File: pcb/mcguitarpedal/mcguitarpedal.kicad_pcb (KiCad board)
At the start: 2 copper layers, 129.5 x 123 mm, 73 parts, among them J1 IN, J10 ENCODER2, J11 ENCODER3, J2 PREAMP_HEADERS, J3 BTN_MTX, J4 OUT, J5 EXP, J6 ILI9488 Module, J7 PWR_IN, J8 POT_HP_VOLUME_10k, J9 ENCODER1, SW1 SW_BYPASS, SW3 SW_PRESET, SW4 LINE_LEVEL, SW5 SW_TUNER, SW6 SW_PRESET, U2 Teensy4.1, U3 LM4562, U4 74HC148, U5 74HC4094, U6 STPDWN-3P-5V, U7 STDN-3A24-ADJ

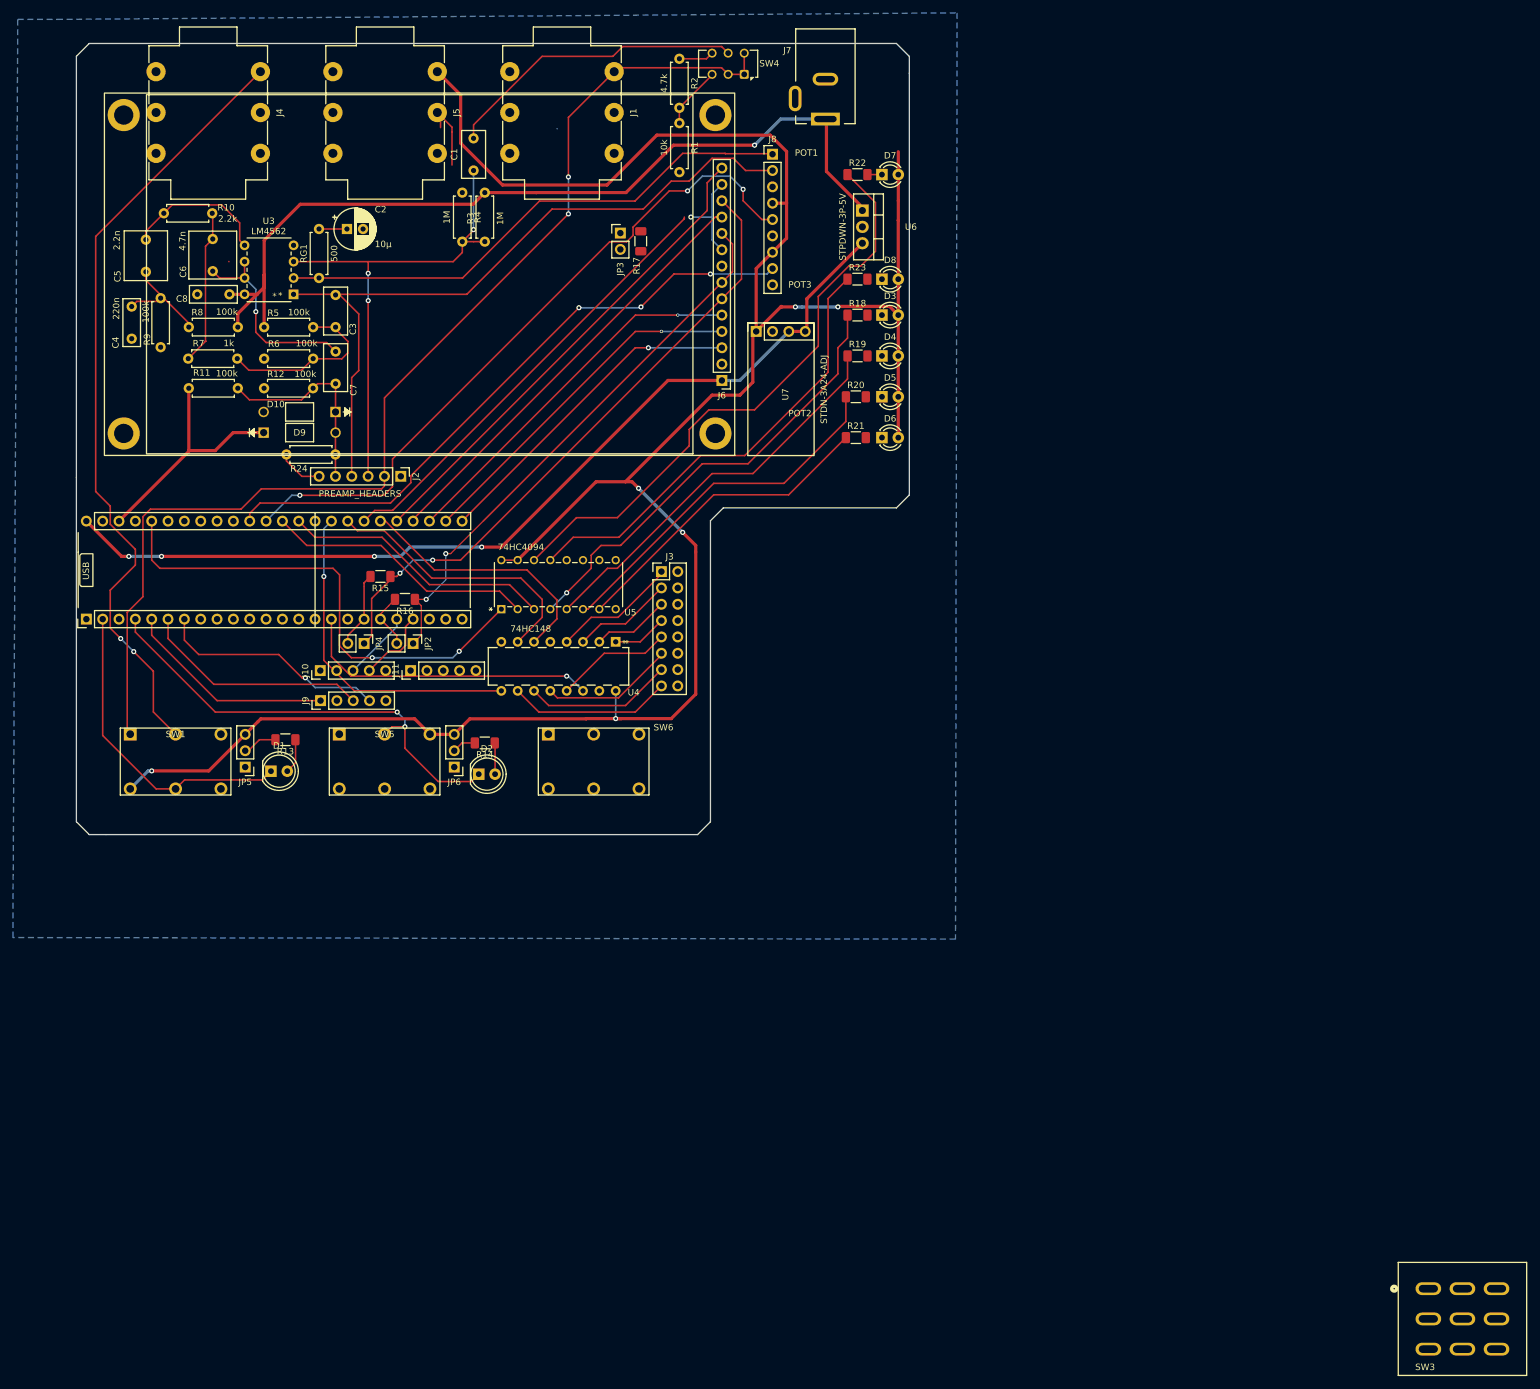
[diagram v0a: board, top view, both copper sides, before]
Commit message: HCT595, audio shield sockets
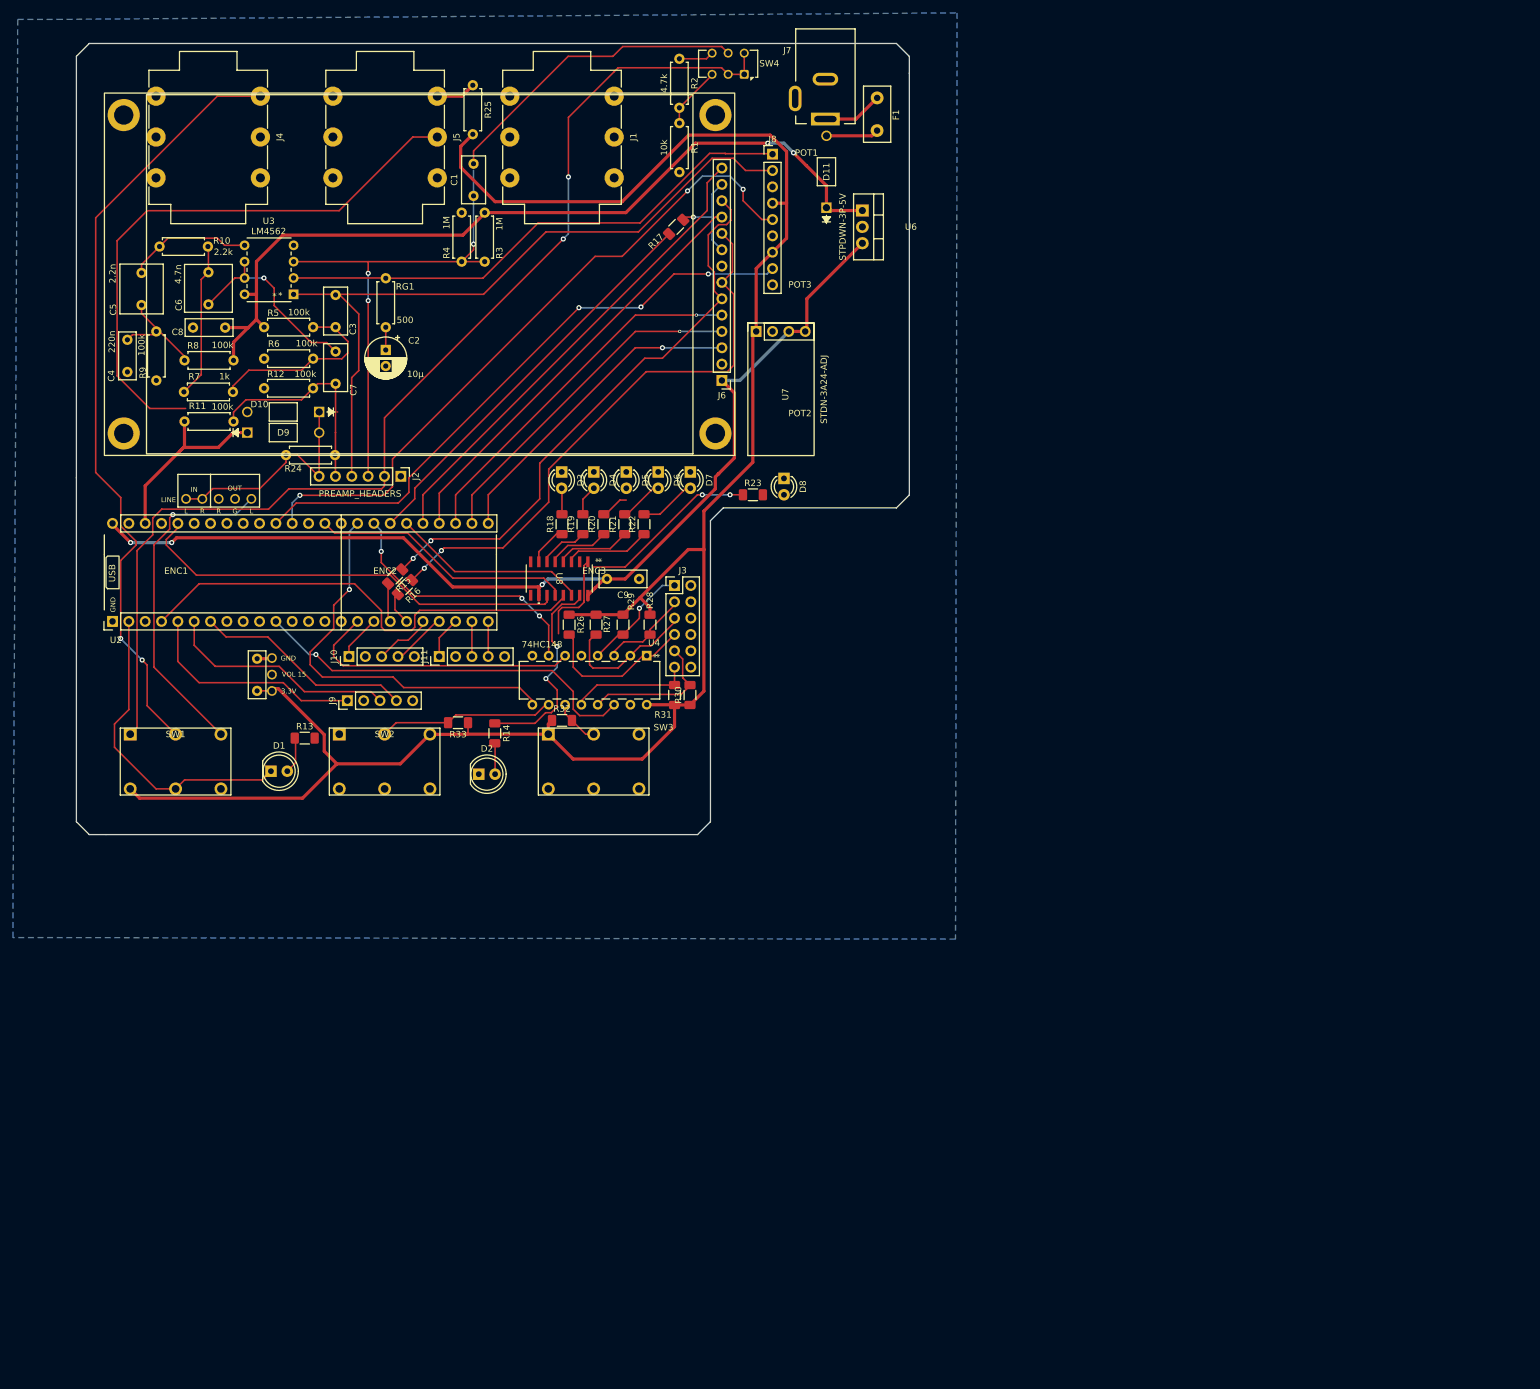
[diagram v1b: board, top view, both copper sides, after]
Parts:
- removed JP2: JP_SCLK, Connector_PinHeader_2.54mm:PinHeader_1x02_P2.54mm_Vertical
- removed JP3: JP_MISO, Connector_PinHeader_2.54mm:PinHeader_1x02_P2.54mm_Vertical
- removed JP4: JP_MOSI, Connector_PinHeader_2.54mm:PinHeader_1x02_P2.54mm_Vertical
- removed JP5, JP6: JP_SW1_LED, Connector_PinHeader_2.54mm:PinHeader_1x03_P2.54mm_Vertical
- removed the R21 at (170.7, 81.3)
- removed the SW3 at (259.7, 213.6)
- removed U5: 74HC4094, TI_FOOTPRINTS:N16
- added C10: 100nf, Capacitor_THT:C_Rect_L7.2mm_W2.5mm_P5.00mm_FKS2_FKP2_MKS2_MKP2, F.Cu at (77.6, 120.7)
- added C9: 100nf, Capacitor_THT:C_Rect_L7.2mm_W2.5mm_P5.00mm_FKS2_FKP2_MKS2_MKP2, F.Cu at (137.0, 103.3)
- added D11: D_Schottky, TI_FOOTPRINTS:DO-41_DIO, F.Cu at (166.1, 45.5)
- added ENC1: Logo_Open_Hardware_Small, mcguitarpedal:Floating Encoder, F.Cu at (65.0, 102.5)
- added ENC2: Logo_Open_Hardware_Small, mcguitarpedal:Floating Encoder, F.Cu at (97.5, 102.5)
- added ENC3: Logo_Open_Hardware_Small, mcguitarpedal:Floating Encoder, F.Cu at (130.0, 102.5)
- added F1: Fuse 1A, Fuse:Fuse_Littelfuse_395Series, F.Cu at (174.0, 28.5)
- added R18: 330, Resistor_SMD:R_1206_3216Metric_Pad1.30x1.75mm_HandSolder, F.Cu at (125.0, 94.7)
- added R25: 1k, Resistor_THT:R_Axial_DIN0207_L6.3mm_D2.5mm_P7.62mm_Horizontal, F.Cu at (111.1, 26.5)
- added R26: 10k, Resistor_SMD:R_1206_3216Metric_Pad1.30x1.75mm_HandSolder, F.Cu at (126.1, 110.4)
- added R27: 10k, Resistor_SMD:R_1206_3216Metric_Pad1.30x1.75mm_HandSolder, F.Cu at (130.3, 110.4)
- added R28: 10k, Resistor_SMD:R_1206_3216Metric_Pad1.30x1.75mm_HandSolder, F.Cu at (138.7, 110.4)
- added R29: 10k, Resistor_SMD:R_1206_3216Metric_Pad1.30x1.75mm_HandSolder, F.Cu at (134.5, 110.4)
- added R30: 10k, Resistor_SMD:R_1206_3216Metric_Pad1.30x1.75mm_HandSolder, F.Cu at (144.9, 121.3)
- added R31: 10k, Resistor_SMD:R_1206_3216Metric_Pad1.30x1.75mm_HandSolder, F.Cu at (142.5, 121.3)
- added R32: 10k, Resistor_SMD:R_1206_3216Metric_Pad1.30x1.75mm_HandSolder, F.Cu at (125.0, 125.2)
- added R33: 10k, Resistor_SMD:R_1206_3216Metric_Pad1.30x1.75mm_HandSolder, F.Cu at (108.8, 125.6)
- added U2: Teensy Audio Board, mcguitarpedal:4.0audioshield, F.Cu at (55.1, 109.9)
- added U8: 74HCT595D, TI_FOOTPRINTS:SOT109-1_NEX, F.Cu at (124.6, 103.2)
- D3, D6, D7, D8: footprint LED_THT:LED_D3.0mm -> mcguitarpedal:LED_D3.0mm
- D4: renamed from D5; footprint LED_THT:LED_D3.0mm -> mcguitarpedal:LED_D3.0mm
- D5: renamed from D4; footprint LED_THT:LED_D3.0mm -> mcguitarpedal:LED_D3.0mm
- J3: footprint Connector_PinHeader_2.54mm:PinHeader_2x08_P2.54mm_Vertical -> Connector_PinHeader_2.54mm:PinHeader_2x06_P2.54mm_Vertical
- J6: footprint ILI9488:ILI9488 -> mcguitarpedal:ILI9488
- R13, R14, R22, R23: value 150 -> 330
- R19: renamed from R20; value 150 -> 330
- R20: renamed from R19; value 150 -> 330
- R21: renamed from R18; value 150 -> 330
- moved R22 63.7 mm to (137.8, 94.7), turned to 90 degrees
- moved D3 55.4 mm to (125.0, 86.6), turned to -90 degrees
- moved D7 55.0 mm to (145.0, 86.6), turned to -90 degrees
- moved R21 48.7 mm to (134.8, 94.7), turned to 90 degrees
- moved R20 47.3 mm to (131.5, 94.7), turned to 90 degrees
- moved R19 46.8 mm to (128.2, 94.7), turned to 90 degrees
- moved D4 46.3 mm to (130.0, 86.6), turned to -90 degrees
- moved D5 43.6 mm to (135.0, 86.6), turned to -90 degrees
- moved R23 37.3 mm to (154.7, 90.2)
- moved D6 35.2 mm to (140.0, 86.6), turned to -90 degrees
- moved D8 34.5 mm to (159.5, 87.6), turned to -90 degrees
- moved C2 19.8 mm to (97.6, 67.7), turned to -90 degrees
- moved RG1 10.4 mm to (97.6, 56.5), turned to -90 degrees
- moved R17 5.94 mm to (142.7, 48.5), turned to -135 degrees
- moved U4 5.29 mm to (138.2, 115.2)
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- renumbered SW5 to SW2, SW6 to SW3, U2 to U1
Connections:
- net Net-(U2-40_A16) renamed /40_BTN_MTX_B
- net Net-(U2-41_A17) renamed /41_BTN_MTX_A
- D1 pad 1: /1_SW1 -> GND
- D10 pad 1: /preamp/PREAMP_OUT -> /LINE_IN
- D2 pad 1: /2_SW2 -> GND
- D3 pad 1: Net-(D3-K) -> GND
- D3 pad 2: 3.3V -> Net-(D3-A)
- D4 pad 1: Net-(D5-K) -> GND
- D4 pad 2: 3.3V -> Net-(D4-A)
- D5 pad 1: Net-(D4-K) -> GND
- D5 pad 2: 3.3V -> Net-(D5-A)
- D6 pad 1: Net-(D6-K) -> GND
- D6 pad 2: 3.3V -> Net-(D6-A)
- D7 pad 1: Net-(D7-K) -> GND
- D7 pad 2: 3.3V -> Net-(D7-A)
- D8 pad 1: Net-(D8-K) -> GND
- D8 pad 2: 3.3V -> Net-(D8-A)
- D9 pad 2: /preamp/PREAMP_OUT -> /LINE_IN
- J5 pad T: 3.3V -> Net-(J5-PadT)
- J7 pad 1: 9V -> Net-(F1-Pad1)
- J7 pad 3: (no net) -> unconnected-(J7-Pad3)
- R14 pad 1: Net-(D2-A) -> Net-(U8-Q0)
- R14 pad 2: Net-(JP6-C) -> Net-(D2-A)
- R19 pad 2: Net-(D5-K) -> Net-(D4-A)
- R20 pad 2: Net-(D4-K) -> Net-(D5-A)
- R21 pad 2: Net-(D3-K) -> Net-(D6-A)
- R22 pad 2: Net-(D7-K) -> Net-(D7-A)
- R23 pad 2: Net-(D8-K) -> Net-(D8-A)
- SW2 pad 2: /2_SW2 -> /SW2
- SW3 pad 1: unconnected-(SW6-A-Pad1) -> 3.3V
- SW3 pad 2: unconnected-(SW6-B-Pad2) -> /SW3
- SW3 pad 3: unconnected-(SW6-C-Pad3) -> GND
- U1 pad 10: Net-(U2-8_TX2_IN1) -> unconnected-(U1-8_TX2_IN1-Pad10)
- U1 pad 11: Net-(U2-9_OUT1C) -> /24_BTN_MTX_GS
- U1 pad 12: Net-(U2-10_CS_MQSR) -> unconnected-(U1-10_CS_MQSR-Pad12)
- U1 pad 13: Net-(U2-11_MOSI_CTX1) -> unconnected-(U1-11_MOSI_CTX1-Pad13)
- U1 pad 14: Net-(U2-12_MISO_MQSL) -> unconnected-(U1-12_MISO_MQSL-Pad14)
- U1 pad 16: /24_BTN_MTX_GS -> /24_BTN_MTX_C
- U1 pad 3: Net-(U2-1_TX1_CTX2_MISO1) -> unconnected-(U1-1_TX1_CTX2_MISO1-Pad3)
- U1 pad 30: Net-(U2-38_CS1_IN1) -> /38_LED_DATA
- U1 pad 36: /LED_DATA -> /14_BACKLIGHT_PWM
- U1 pad 4: /2_SW2 -> /2_LED_PWM
- U1 pad 8: Net-(U2-6_OUT1D) -> unconnected-(U1-6_OUT1D-Pad8)
- U1 pad 9: Net-(U2-7_RX2_OUT1A) -> unconnected-(U1-7_RX2_OUT1A-Pad9)
- U4 pad 10: Net-(J3-Pin_15) -> /SW2
- U4 pad 11: Net-(J3-Pin_13) -> /SW3
- U4 pad 15: GND -> unconnected-(U4-EO-Pad15)
- U4 pad 6: Net-(U2-38_CS1_IN1) -> /24_BTN_MTX_C
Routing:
- net Net-(U8-Q3): track 93.0 -> 13.4 mm
- net /A3_EXP: track 11.3 -> 90.2 mm
- net /2_LED_PWM: track 0.00 -> 73.0 mm
- net /2_SW2: track 71.7 -> 0.00 mm, vias 2 -> 0
- net Net-(U8-Q4): track 70.8 -> 11.7 mm, vias 1 -> 0
- net 3.3V: track 370.7 -> 312.7 mm, vias 6 -> 0
- net /LINE_OUT: track 0.00 -> 52.9 mm, vias 0 -> 1
- net Net-(U8-Q5): track 62.1 -> 9.68 mm
- net Net-(U5-QP3): track 49.4 -> 0.00 mm
- net Net-(U8-Q6): track 56.8 -> 8.39 mm
- net /24_BTN_MTX_C: track 0.00 -> 44.2 mm
- net Net-(U8-Q2): track 71.0 -> 28.0 mm, vias 0 -> 2
- net /LED_DATA: track 42.3 -> 0.00 mm
- net Net-(U2-38_CS1_IN1): track 40.5 -> 0.00 mm
- net Net-(U8-Q0): track 0.00 -> 32.8 mm, vias 0 -> 2
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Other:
- board text added: "TODO: Audio board sockets for line in/out and 3V3 PWR LEDs LED PWM Testpoints Mounting holes Footswitch pushbutton Move 5V regulator above U5 Change diode footprint Header silkscreen labels Move jacks down to reduce board size vertically Move Teensy right to reduce board size horizontally Use SMD HC148? Use HCT595 instead of 4094 Route SW2 to BTN_MTX Decoupling caps for U4-7"
- board text removed: "TODO: Audio board 3V3 PWR LEDs Testpoints Encoders Evenly distribute jacks Mounting holes Footswitch pushbutton Switch 470n to smaller footprint Move 5V regulator above U5"

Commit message: Miniaturization
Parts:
- added R34: 10k, Resistor_SMD:R_1206_3216Metric_Pad1.30x1.75mm_HandSolder, F.Cu at (70.8, 46.5)
- added R35: 10k, Resistor_SMD:R_1206_3216Metric_Pad1.30x1.75mm_HandSolder, F.Cu at (58.0, 49.0)
- added SW5: SW_PWR, Connector_PinHeader_2.54mm:PinHeader_1x02_P2.54mm_Vertical, F.Cu at (166.2, 25.2)
- R1: footprint Resistor_THT:R_Axial_DIN0207_L6.3mm_D2.5mm_P7.62mm_Horizontal -> Resistor_SMD:R_1206_3216Metric_Pad1.30x1.75mm_HandSolder
- R2: value 4.7k -> 10k; footprint Resistor_THT:R_Axial_DIN0207_L6.3mm_D2.5mm_P7.62mm_Horizontal -> Resistor_SMD:R_1206_3216Metric_Pad1.30x1.75mm_HandSolder
- SW4: footprint Button_Switch_THT:SW_CK_JS202011AQN_DPDT_Angled -> mcguitarpedal:DP3T slide switch
- U6: footprint Package_TO_SOT_THT:TO-220-3_Vertical -> Package_TO_SOT_THT:TO-220-3_Horizontal_TabDown
- moved SW4 95.5 mm to (61.2, 49.9), turned to 90 degrees
- moved R2 87.7 mm to (58.0, 43.0)
- moved R1 85.4 mm to (58.0, 37.5)
- moved R23 57.7 mm to (176.0, 36.5), turned to 90 degrees
- moved D8 57.6 mm to (173.5, 31.7), turned to 0 degrees
- moved R25 51.4 mm to (162.0, 34.2)
- moved C1 35.8 mm to (76.4, 52.0), turned to 180 degrees
- moved R3 23.3 mm to (90.0, 49.8)
- moved D9 20.4 mm to (57.2, 88.4)
- moved D10 20.4 mm to (68.4, 85.0)
- moved R4 13.0 mm to (96.9, 57.4)
- moved J4 12.1 mm to (90.2, 27.9)
- moved C4 12.0 mm to (66.2, 74.2), turned to 180 degrees
- moved J5 8.59 mm to (114.2, 28.2)
- moved R9 7.31 mm to (67.5, 69.5), turned to 180 degrees
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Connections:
- C1 pad 2: Net-(C1-Pad2) -> Net-(SW4-D)
- F1 pad 1: Net-(F1-Pad1) -> Net-(SW5-B)
- J7 pad 1: Net-(F1-Pad1) -> Net-(SW5-A)
- R1 pad 1: Net-(R1-Pad1) -> GND
- R1 pad 2: GND -> Net-(R1-Pad2)
- R2 pad 1: Net-(R2-Pad1) -> Net-(R1-Pad2)
- R2 pad 2: Net-(R1-Pad1) -> Net-(R2-Pad2)
- SW4 pad 2: /SIGNAL_IN -> Net-(SW4-D)
- SW4 pad 3: Net-(R1-Pad1) -> Net-(R1-Pad2)
- SW4 pad 4: Net-(R2-Pad1) -> Net-(SW4-D)
- SW4 pad 5: Net-(C1-Pad2) -> Net-(R34-Pad1)
- SW4 pad 6: /SIGNAL_IN -> Net-(R2-Pad2)
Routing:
- net 3.3V: track 312.7 -> 243.5 mm
- net Net-(U8-Q2): track 28.0 -> 91.6 mm
- net /SIGNAL_IN: track 176.6 -> 238.4 mm
- net Net-(C1-Pad2): track 48.7 -> 0.00 mm
- net Net-(U8-Q1): track 14.6 -> 62.2 mm, vias 0 -> 4
- net Net-(J5-PadT): track 6.23 -> 53.4 mm
- net /preamp/STAGE1_IN: track 78.0 -> 53.1 mm
- net Net-(SW4-D): track 0.00 -> 23.2 mm, vias 0 -> 1
- net /SIGNAL_OUT: track 120.9 -> 139.7 mm
- net Net-(R34-Pad1): track 0.00 -> 17.7 mm
- net /1_SW1: track 48.6 -> 32.7 mm
- net Net-(R2-Pad2): track 0.00 -> 13.8 mm
- net Net-(SW5-A): track 0.00 -> 11.4 mm
- net Net-(R1-Pad1): track 9.57 -> 0.00 mm
- net Net-(F1-Pad1): track 9.47 -> 0.00 mm
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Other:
- board text added: "TODO: PWR LEDs Testpoints Mounting holes Header silkscreen labels Decoupling caps for U4-7 (SMD ceramic?)"
- board text removed: "TODO: Audio board sockets for line in/out and 3V3 PWR LEDs LED PWM Testpoints Mounting holes Footswitch pushbutton Move 5V regulator above U5 Change diode footprint Header silkscreen labels Move jacks down to reduce board size vertically Move Teensy right to reduce board size horizontally Use SMD HC148? Use HCT595 instead of 4094 Route SW2 to BTN_MTX Decoupling caps for U4-7"
